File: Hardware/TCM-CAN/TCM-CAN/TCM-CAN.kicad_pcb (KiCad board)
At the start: 2 copper layers, 4 parts, among them J2 Conn_01x27_Socket, J3 Conn_01x27_Socket, J4 Conn_02x20_Odd_Even, J5 Conn_01x06_Socket

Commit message: started work on the PCB for TCM-CAN
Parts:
- moved J3 79.1 mm to (132.2, 39.8)
- moved J4 71.1 mm to (127.7, 54.0)
- moved J2 65.8 mm to (114.2, 39.8)
- moved J5 50.1 mm to (116.7, 33.0)
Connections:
- J2 pad 1: +12V -> 12V
- J2 pad 11: CANL2 -> CAN1_N
- J2 pad 12: CANH2 -> CAN1_P
- J2 pad 20: SPI1_MISO -> SPI_MISO
- J2 pad 21: SPI1_MOSI -> SPI_MOSI
- J2 pad 22: SPI1_SCK -> SPI_SCK
- J2 pad 23: PA4 -> SPI_CS
- J3 pad 1: +12V -> 12V
- J3 pad 8: CANH3 -> CAN2_P
- J3 pad 9: CANL3 -> CAN2_N
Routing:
- added copper zone on F.Cu, net (none)
- added copper zone on B.Cu, net GND
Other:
- board outline added: 22.9 x 79.5 mm

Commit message: Finished TCM-CAN pcb need to order it and get it drc'd
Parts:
- added G***: LOGO, LOGO:grloho, F.Cu at (119.7, 98.1)
- added JP1: SolderJumper_2_Open, Jumper:SolderJumper-2_P1.3mm_Open_Pad1.0x1.5mm, B.Cu at (123.6, 39.2)
- added JP2: SolderJumper_2_Open, Jumper:SolderJumper-2_P1.3mm_Open_Pad1.0x1.5mm, B.Cu at (121.6, 48.1)
- moved J3 18.0 mm to (114.2, 39.8)
- moved J2 18.0 mm to (132.2, 39.8)
- moved J5 12.5 mm to (129.2, 33.0), turned to 180 degrees
- moved J4 1.97 mm to (128.1, 52.1)
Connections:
- J2 pad 1: 12V -> +12V
- J3 pad 1: 12V -> +12V
- J5 pad 3: CAN1_P -> CAN1_N
- J5 pad 4: CAN1_N -> CAN1_P
- J5 pad 5: CAN2_P -> CAN2_N
- J5 pad 6: CAN2_N -> CAN2_P
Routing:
- net CAN1_P: track 0.00 -> 39.1 mm
- net CAN1_N: track 0.00 -> 35.5 mm
- net CAN2_N: track 0.00 -> 29.2 mm
- net 3v3: track 0.00 -> 29.2 mm
- net SPI_SCK: track 0.00 -> 27.5 mm
- net CAN2_P: track 0.00 -> 26.2 mm
- net +12V: track 0.00 -> 18.0 mm
- net +3.3V: track 0.00 -> 18.0 mm
- net GND: track 0.00 -> 16.7 mm, vias 0 -> 33
- net SPI_MISO: track 0.00 -> 14.6 mm
- net SPI_CS: track 0.00 -> 9.76 mm
- net SPI_MOSI: track 0.00 -> 8.88 mm
- net 12V: track 0.00 -> 7.00 mm
- added copper zone on F.Cu, net GND
- removed copper zone on F.Cu, net (none)
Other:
- board text added: "Solder for 12V ↑ power from car."
- board text added: "Solder for 3.3v from jetson DO NOT SOLDER BOTH"

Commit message: tcm-can pcb done
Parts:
- J4: moved to B.Cu
- moved J4 2.51 mm to (125.6, 52.2), turned to 180 degrees
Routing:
- net GND: track 16.7 -> 0.00 mm
- net SPI_MISO: track 14.6 -> 12.1 mm
- net SPI_SCK: track 27.5 -> 29.8 mm
- net SPI_MOSI: track 8.88 -> 11.1 mm
- net 3v3: track 29.2 -> 27.3 mm
- net SPI_CS: track 9.76 -> 11.1 mm
- net 12V: track 7.00 -> 7.88 mm
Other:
- board text added: "BK is Btard"

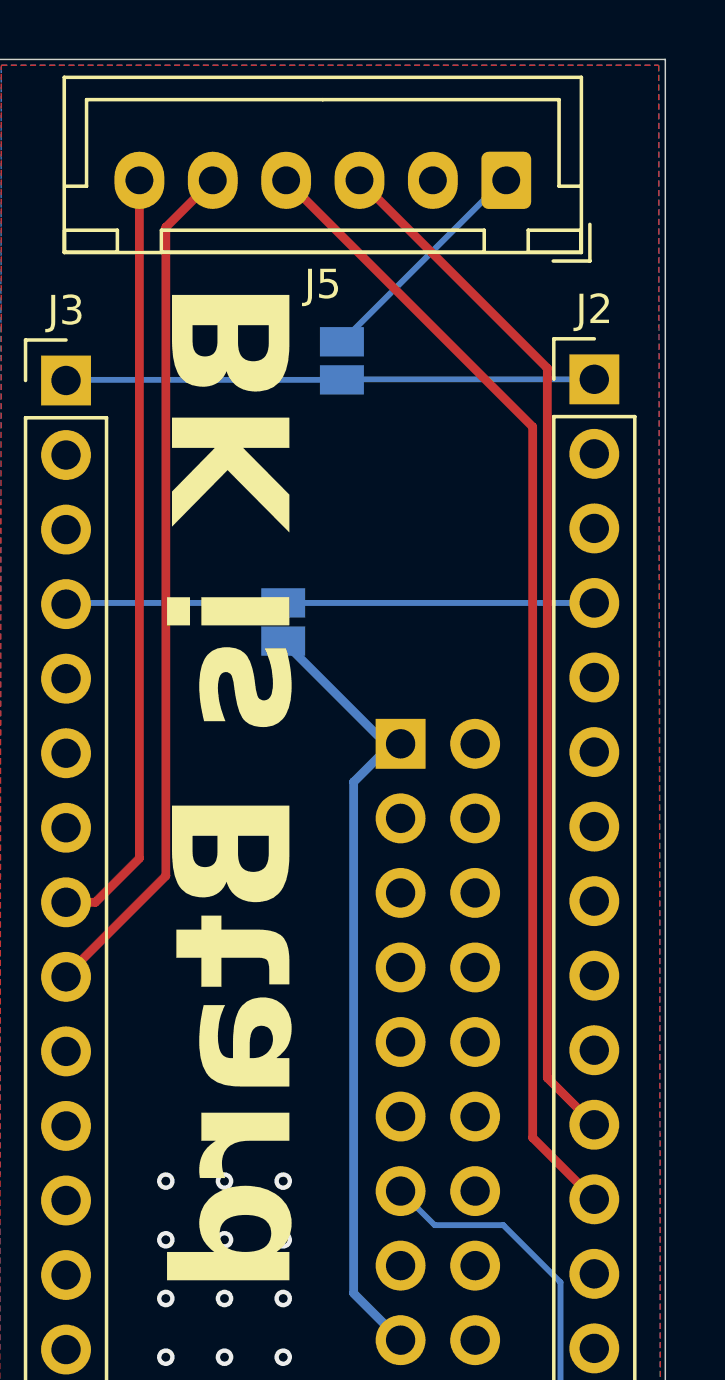
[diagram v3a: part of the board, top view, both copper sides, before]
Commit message: fixed pin names
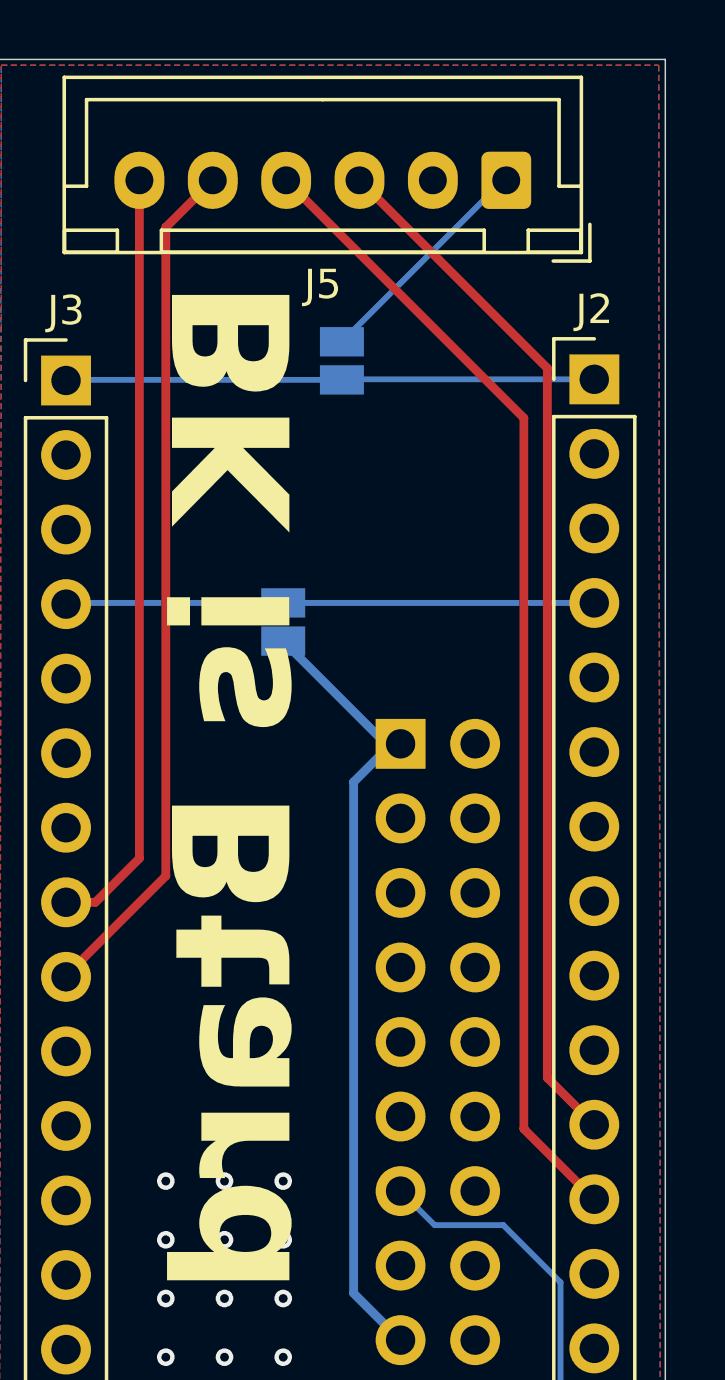
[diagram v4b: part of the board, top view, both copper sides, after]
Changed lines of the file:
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@@
 	)
 	(segment
-		(start 130.58 63.6)
-		(end 132.18 65.2)
+		(start 130.58 39.42)
+		(end 130.58 63.6)
 		(width 0.3)
 		(layer "F.Cu")
@@
 	)
 	(segment
-		(start 130.58 39.42)
-		(end 130.58 63.6)
+		(start 130.58 63.6)
+		(end 132.18 65.2)
 		(width 0.3)
 		(layer "F.Cu")
@@
 	)
 	(segment
-		(start 130.08 41.42)
-		(end 130.08 65.64)
+		(start 129.78 41.12)
+		(end 129.78 65.34)
 		(width 0.3)
 		(layer "F.Cu")
@@
 	(segment
 		(start 121.68 33.02)
-		(end 130.08 41.42)
+		(end 129.78 41.12)
 		(width 0.3)
 		(layer "F.Cu")
@@
 	)
 	(segment
-		(start 130.08 65.64)
+		(start 129.78 65.34)
 		(end 132.18 67.74)
 		(width 0.3)
